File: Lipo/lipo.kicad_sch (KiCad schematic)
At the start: 22 parts, among them J1 Conn_01x10, J2 Conn_01x03_Pin, U1 DMG6968U-7, U2 DMG6968U-7, U3 MCP1825S, U4 MCP73831-2-OT, U5 AP9101CK

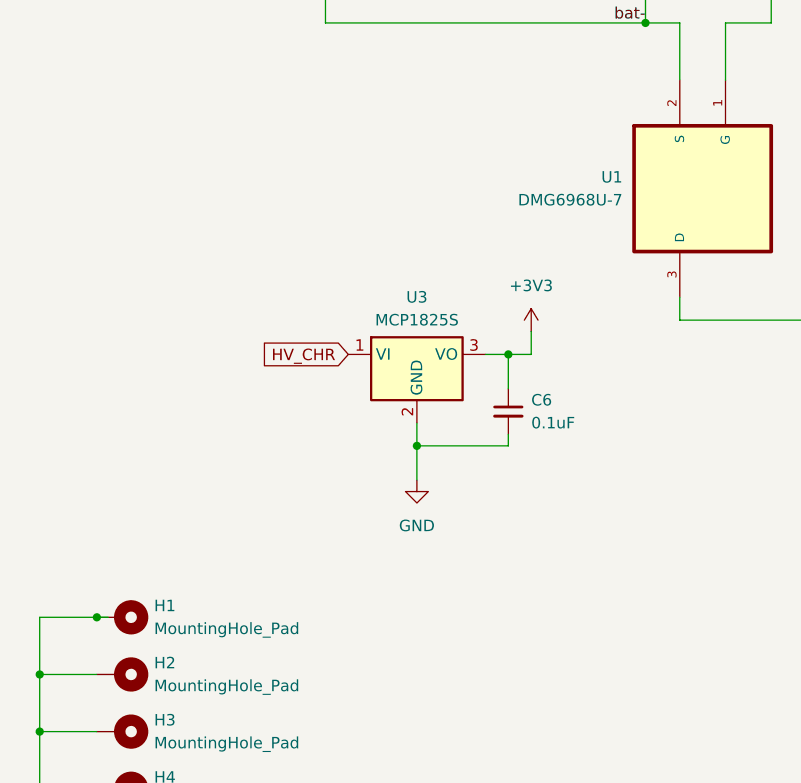
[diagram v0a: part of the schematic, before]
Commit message: resolved erc errors in lip and added footprint
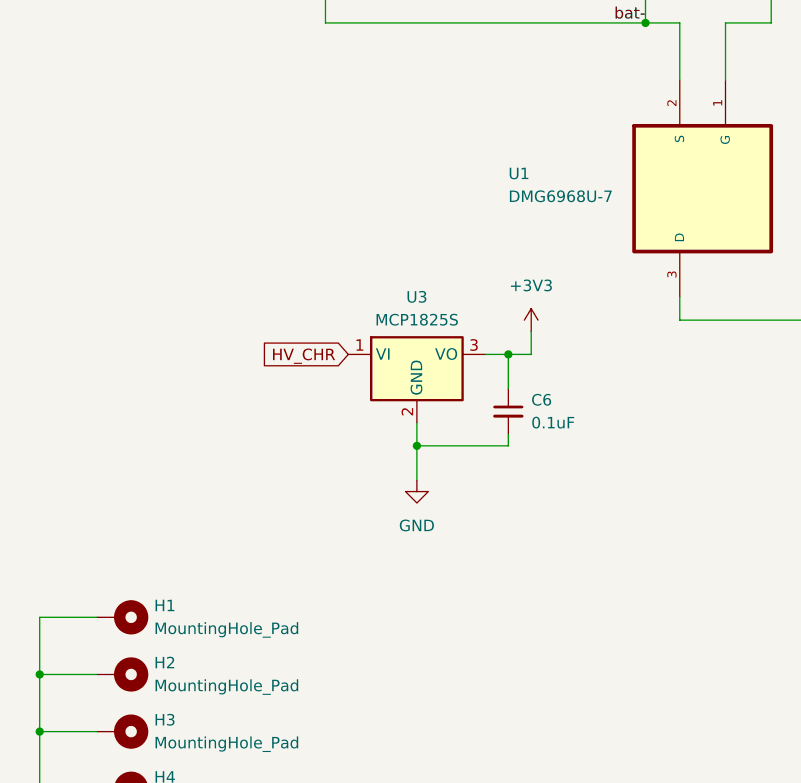
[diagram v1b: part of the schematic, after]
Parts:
- BT1: footprint (none) -> Connector_PinHeader_2.54mm:PinHeader_1x02_P2.54mm_Vertical_SMD_Pin1Left
- C6, C7, C8: footprint (none) -> Capacitor_SMD:C_0201_0603Metric
- D88: footprint (none) -> LED_SMD:LED_0603_1608Metric
- H1, H2, H3, H4, H5, H6: footprint (none) -> MountingHole:MountingHole_3.2mm_M3_DIN965_Pad
- J1: footprint (none) -> Connector_FFC-FPC:Molex_200528-0100_1x10-1MP_P1.00mm_Horizontal
- J2: footprint (none) -> Connector_PinHeader_2.54mm:PinHeader_1x03_P2.54mm_Vertical_SMD_Pin1Left
- R5, R6, R7, R8: footprint (none) -> Resistor_SMD:R_0201_0603Metric
- U1, U2: footprint DMG6968U-7:SOT95P240X110-3N -> Library:dmg6968U7
- U3: footprint (none) -> Package_TO_SOT_SMD:SOT-223-3_TabPin2
